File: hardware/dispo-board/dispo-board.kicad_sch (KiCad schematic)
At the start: 32 parts, among them SW1 SW_Push, U1 TPS79633DCQ, U2 STM32H725RGV6, Y1 32M

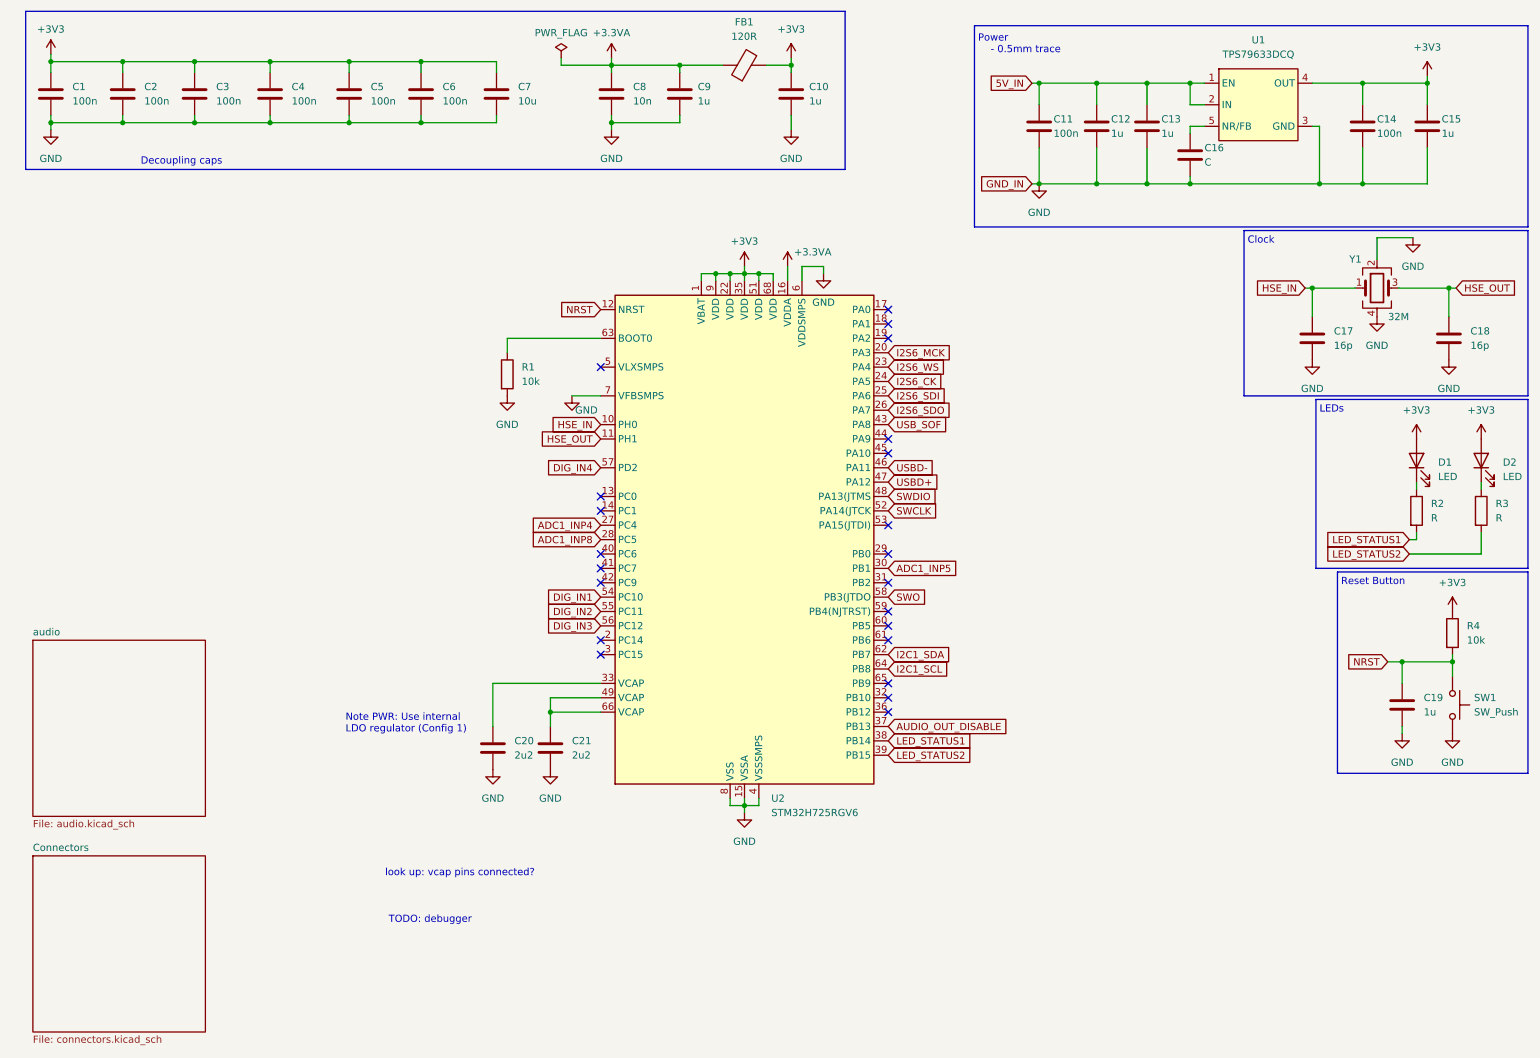
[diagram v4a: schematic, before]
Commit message: added footprints and mouser nrs
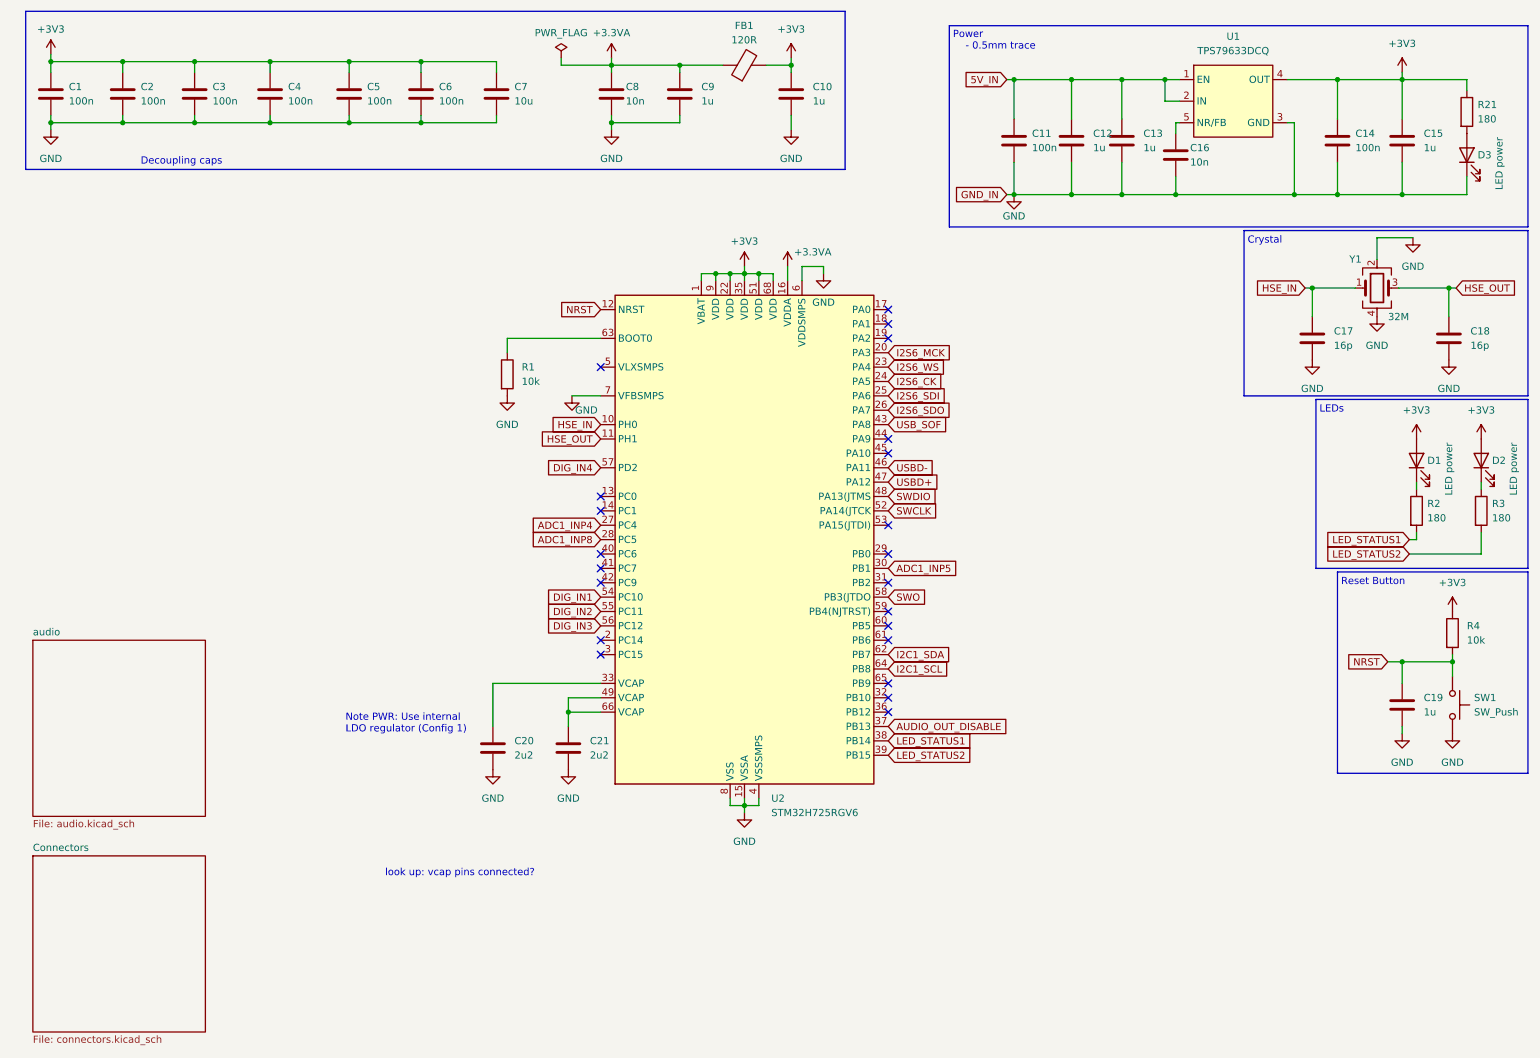
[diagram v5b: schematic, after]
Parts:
- added D3: LED power, LED_SMD:LED_0603_1608Metric, symbol Device:LED
- added R21: 180, Resistor_SMD:R_0603_1608Metric, symbol Device:R
- C1, C11, C14, C2, C3, C4, C5, C6: footprint (none) -> Capacitor_SMD:C_0402_1005Metric; MOUSER_NR (none) -> 81-GRM15R61A104KA01J
- C10, C12, C13, C15, C19, C9: footprint (none) -> Capacitor_SMD:C_0603_1608Metric; MOUSER_NR (none) -> 81-GRM185R61C105KE4J
- C16: value C -> 10n; footprint (none) -> Capacitor_SMD:C_0402_1005Metric; MOUSER_NR (none) -> 81-GRM1555CYA103GE1D
- C17, C18: footprint (none) -> Capacitor_SMD:C_0402_1005Metric; MOUSER_NR (none) -> 81-GRM1555C1H160GA1D
- C20, C21: footprint (none) -> Capacitor_SMD:C_0603_1608Metric; MOUSER_NR (none) -> 81-GRM188R71A225KE5J
- C7: footprint (none) -> Capacitor_SMD:C_0603_1608Metric; MOUSER_NR (none) -> 81-GRM188C81A106MA3D
- C8: footprint (none) -> Capacitor_SMD:C_0402_1005Metric; MOUSER_NR (none) -> 81-GRM1555CYA103GE1D
- D1, D2: value LED -> LED power; footprint (none) -> LED_SMD:LED_0603_1608Metric; MOUSER_NR (none) -> 645-598-8N80-107F
- FB1: footprint (none) -> Resistor_SMD:R_0402_1005Metric; MOUSER_NR (none) -> 81-BLM15PX121SH1D
- R1, R4: footprint (none) -> Resistor_SMD:R_0402_1005Metric; MOUSER_NR (none) -> 71-CRCW040210K0FKEDC
- R2, R3: value R -> 180; footprint (none) -> Resistor_SMD:R_0603_1608Metric; MOUSER_NR (none) -> 652-CR0603JW-181ELF
- SW1: footprint (none) -> Button_Switch_SMD:SW_Push_1P1T_NO_6x6mm_H9.5mm; MOUSER_NR (none) -> 506-FSM2JSMAATR
- Y1: MOUSER_NR (none) -> 815-11W32-8D1XT
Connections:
- net +3V3: now also R21.1
- net GND: now also D3.1 (K)
- new net: D3.2 (A), R21.2
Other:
- note added: "Crystal"
- note removed: "Clock"
- note removed: "TODO: debugger"
- moved on the sheet: C16, U1

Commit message: few changes supply op amp, anaolg input and output, updated footprints and mouser nrs
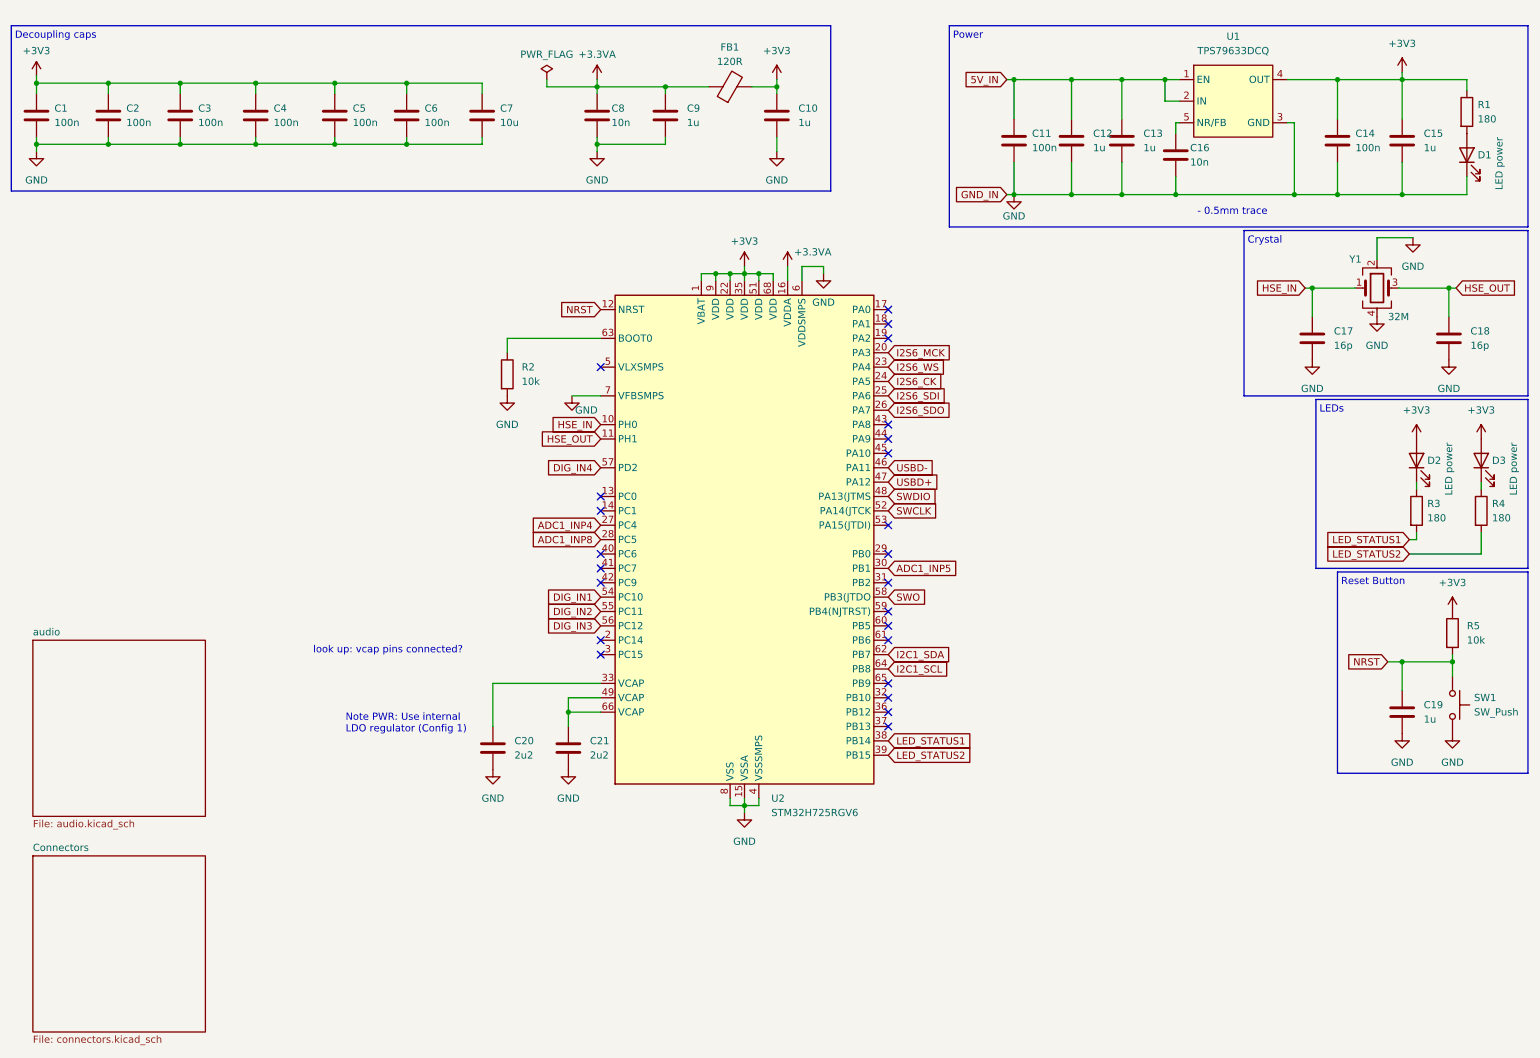
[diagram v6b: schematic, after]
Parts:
- renumbered D3 to D1, D1 to D2, D2 to D3, R21 to R1, R1 to R2, R2 to R3, R3 to R4, R4 to R5
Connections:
- net AUDIO_OUT_DISABLE: no longer names the net of U2.37 (PB13)
- net USB_SOF: no longer names the net of U2.43 (PA8)
- no-connect marks 22 -> 24
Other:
- note added: "- 0.5mm trace"
- note added: "Power"
- note removed: "Power - 0.5mm trace"
- moved on the sheet: C1, C10, C19, C2, C3, C4, C5, C6, C7, C8, C9, FB1

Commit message: updated footprints, pcb
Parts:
- removed C12, C13: 1u, Capacitor_SMD:C_0603_1608Metric, symbol Device:C
- C11: value 100n -> 2u2; footprint Capacitor_SMD:C_0402_1005Metric -> Capacitor_SMD:C_0603_1608Metric; MOUSER_NR 81-GRM15R61A104KA01J -> 81-GRM188R71A225KE5J
- renumbered C14 to C12, C15 to C13, C16 to C14, C17 to C15, C18 to C16, C19 to C17, C20 to C18, C21 to C19

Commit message: pcb and parts ordered like this
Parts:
- U1: MOUSER_NO 595-TPS79633DCQ -> (none); MOUSER_NR (none) -> 595-TPS79633DCQ
